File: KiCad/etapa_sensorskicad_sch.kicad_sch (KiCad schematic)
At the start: 15 parts, among them K1 Fujitsu_FTR-LYAA005x, K2 Fujitsu_FTR-LYAA005x, Q1 IRLIZ44N, U1 FDC2214, U2 FXTH87

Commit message: MANTECAMANTECOSA
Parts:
- renumbered U1 to U6, U2 to U7
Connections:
- net at U6.10 (IN0B): now also C3.1, L1.1
- net at U6.9 (IN0A): now also C3.2, L1.2
- net Vcc_12V renamed +12V
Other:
- moved on the sheet: C3, L1

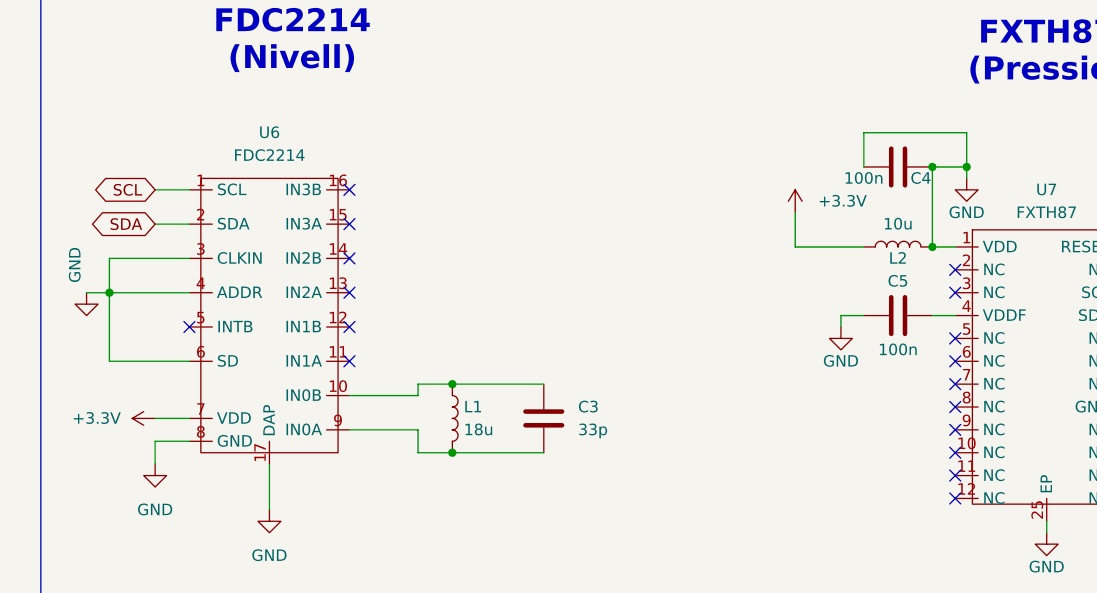
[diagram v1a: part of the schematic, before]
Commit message: GNDs, VCCs col.locats correctament, pull-ups, etc ben connectats
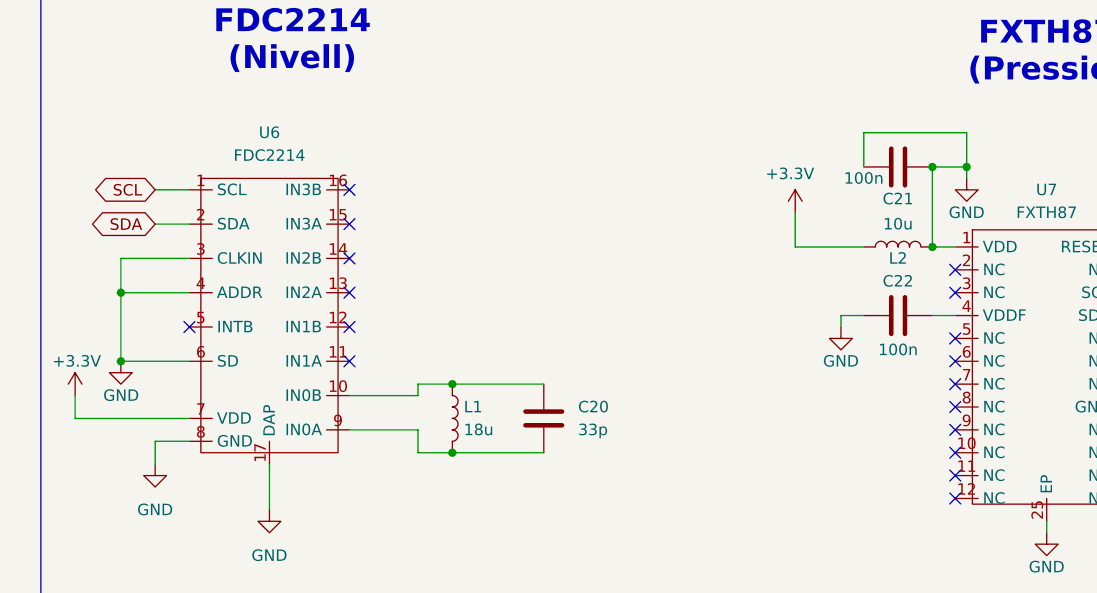
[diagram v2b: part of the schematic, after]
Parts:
- renumbered C3 to C20, C4 to C21, C5 to C22
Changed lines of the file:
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@@
+	)
+	(junction
+		(at 24.13 68.58)
+		(diameter 0)
+		(color 0 0 0 0)
 	)
 	(junction
@@
 	)
 	(junction
+		(at 24.13 60.96)
+		(diameter 0)
+		(color 0 0 0 0)
+	)
+	(junction
 		(at 118.11 46.99)
 		(diameter 0)
@@
 		(color 0 0 0 0)
 	)
-	(junction
-		(at 22.86 60.96)
-		(diameter 0)
-		(color 0 0 0 0)
-	)
 	(no_connect
 		(at 116.84 81.28)
@@
 	(wire
 		(pts
+			(xy 19.05 72.39) (xy 19.05 74.93)
+		)
+		(stroke
+			(width 0)
+			(type default)
+		)
+	)
+	(wire
+		(pts
 			(xy 226.06 139.7) (xy 251.46 139.7)
 		)
@@
 	(wire
 		(pts
-			(xy 31.75 68.58) (xy 22.86 68.58)
+			(xy 31.75 68.58) (xy 24.13 68.58)
 		)
 		(stroke
@@
 	(wire
 		(pts
-			(xy 31.75 57.15) (xy 22.86 57.15)
-		)
-		(stroke
-			(width 0)
-			(type default)
-		)
-	)
-	(wire
-		(pts
-			(xy 22.86 60.96) (xy 22.86 68.58)
+			(xy 31.75 57.15) (xy 24.13 57.15)
 		)
 		(stroke
@@
 	(wire
 		(pts
-			(xy 20.32 60.96) (xy 22.86 60.96)
+			(xy 24.13 60.96) (xy 24.13 68.58)
 		)
 		(stroke
@@
 	(wire
 		(pts
+			(xy 19.05 74.93) (xy 31.75 74.93)
+		)
+		(stroke
+			(width 0)
+			(type default)
+		)
+	)
+	(wire
+		(pts
 			(xy 99.06 52.07) (xy 99.06 55.88)
 		)
@@
 	(wire
 		(pts
-			(xy 22.86 57.15) (xy 22.86 60.96)
+			(xy 24.13 57.15) (xy 24.13 60.96)
 		)
 		(stroke
@@
 		)
 	)
+	(wire
+		(pts
+			(xy 24.13 60.96) (xy 31.75 60.96)
+		)
+		(stroke
+			(width 0)
+			(type default)
+		)
+	)
 	(bus
 		(pts
@@
 	(wire
 		(pts
-			(xy 27.94 74.93) (xy 31.75 74.93)
-		)
-		(stroke
-			(width 0)
-			(type default)
-		)
-	)
-	(wire
-		(pts
 			(xy 201.93 54.61) (xy 214.63 54.61)
 		)
@@
 		(pts
 			(xy 201.93 77.47) (xy 208.28 77.47)
-		)
-		(stroke
-			(width 0)
-			(type default)
-		)
-	)
-	(wire
-		(pts
-			(xy 22.86 60.96) (xy 31.75 60.96)
 		)
 		(stroke
@@
 		(on_board yes)
 		(dnp no)
-		(property "Reference" "C5"
+		(property "Reference" "C22"
 			(at 110.49 59.69 90)
 			(effects
@@
 			(project ""
 				(path "/27a7fca5-115a-450a-aa60-496c314f6c0e/214c85b5-e11a-40fa-b086-a325260ddb4b"
-					(reference "C5")
+					(reference "C22")
 					(unit 1)
 				)
@@
 		(on_board yes)
 		(dnp no)
-		(fields_autoplaced yes)
 		(property "Reference" "#PWR0121"
 			(at 99.06 55.88 0)
@@
 		)
 		(property "Value" "+3.3V"
-			(at 101.6 50.7999 0)
+			(at 95.758 47.752 0)
 			(effects
 				(font
@@
 	(symbol
 		(lib_id "power:GND")
-		(at 20.32 60.96 0)
+		(at 24.13 68.58 0)
 		(unit 1)
 		(exclude_from_sim no)
@@
 		(dnp no)
 		(property "Reference" "#PWR0109"
-			(at 20.32 67.31 0)
+			(at 24.13 74.93 0)
 			(effects
 				(font
@@
 		)
 		(property "Value" "GND"
-			(at 19.05 55.88 90)
+			(at 26.162 72.39 0)
 			(effects
 				(font
@@
 		)
 		(property "Footprint" ""
-			(at 20.32 60.96 0)
+			(at 24.13 68.58 0)
 			(effects
 				(font
@@
 		)
 		(property "Datasheet" ""
-			(at 20.32 60.96 0)
+			(at 24.13 68.58 0)
 			(effects
 				(font
@@
 		)
 		(property "Description" "Power symbol creates a global label with name \"GND\" , ground"
-			(at 20.32 60.96 0)
+			(at 24.13 68.58 0)
 			(effects
 				(font
@@
 		(dnp no)
 		(fields_autoplaced yes)
-		(property "Reference" "C3"
+		(property "Reference" "C20"
 			(at 74.93 73.6599 0)
 			(effects
@@
 			(project ""
 				(path "/27a7fca5-115a-450a-aa60-496c314f6c0e/214c85b5-e11a-40fa-b086-a325260ddb4b"
-					(reference "C3")
+					(reference "C20")
 					(unit 1)
 				)
@@
 		(on_board yes)
 		(dnp no)
-		(property "Reference" "C4"
-			(at 113.03 48.26 90)
+		(property "Reference" "C21"
+			(at 110.49 50.546 90)
 			(effects
 				(font
@@
 			(project "PROJECTE_CASTRO_RIBAS"
 				(path "/27a7fca5-115a-450a-aa60-496c314f6c0e/214c85b5-e11a-40fa-b086-a325260ddb4b"
-					(reference "C4")
+					(reference "C21")
 					(unit 1)
 				)
@@
 	(symbol
 		(lib_id "power:+3.3V")
-		(at 27.94 74.93 90)
+		(at 19.05 72.39 0)
 		(unit 1)
 		(exclude_from_sim no)
@@
 		(on_board yes)
 		(dnp no)
-		(fields_autoplaced yes)
 		(property "Reference" "#PWR0110"
-			(at 31.75 74.93 0)
+			(at 19.05 76.2 0)
 			(effects
 				(font
@@
 		)
 		(property "Value" "+3.3V"
-			(at 24.13 74.9299 90)
+			(at 16.51 68.58 0)
 			(effects
 				(font
@@
 		)
 		(property "Footprint" ""
-			(at 27.94 74.93 0)
+			(at 19.05 72.39 0)
 			(effects
 				(font
@@
 		)
 		(property "Datasheet" ""
-			(at 27.94 74.93 0)
+			(at 19.05 72.39 0)
 			(effects
 				(font
@@
 		)
 		(property "Description" "Power symbol creates a global label with name \"+3.3V\""
-			(at 27.94 74.93 0)
-			(effects
-				(font
+			(at 19.05 72.39 0)
+			(effects
+				(font

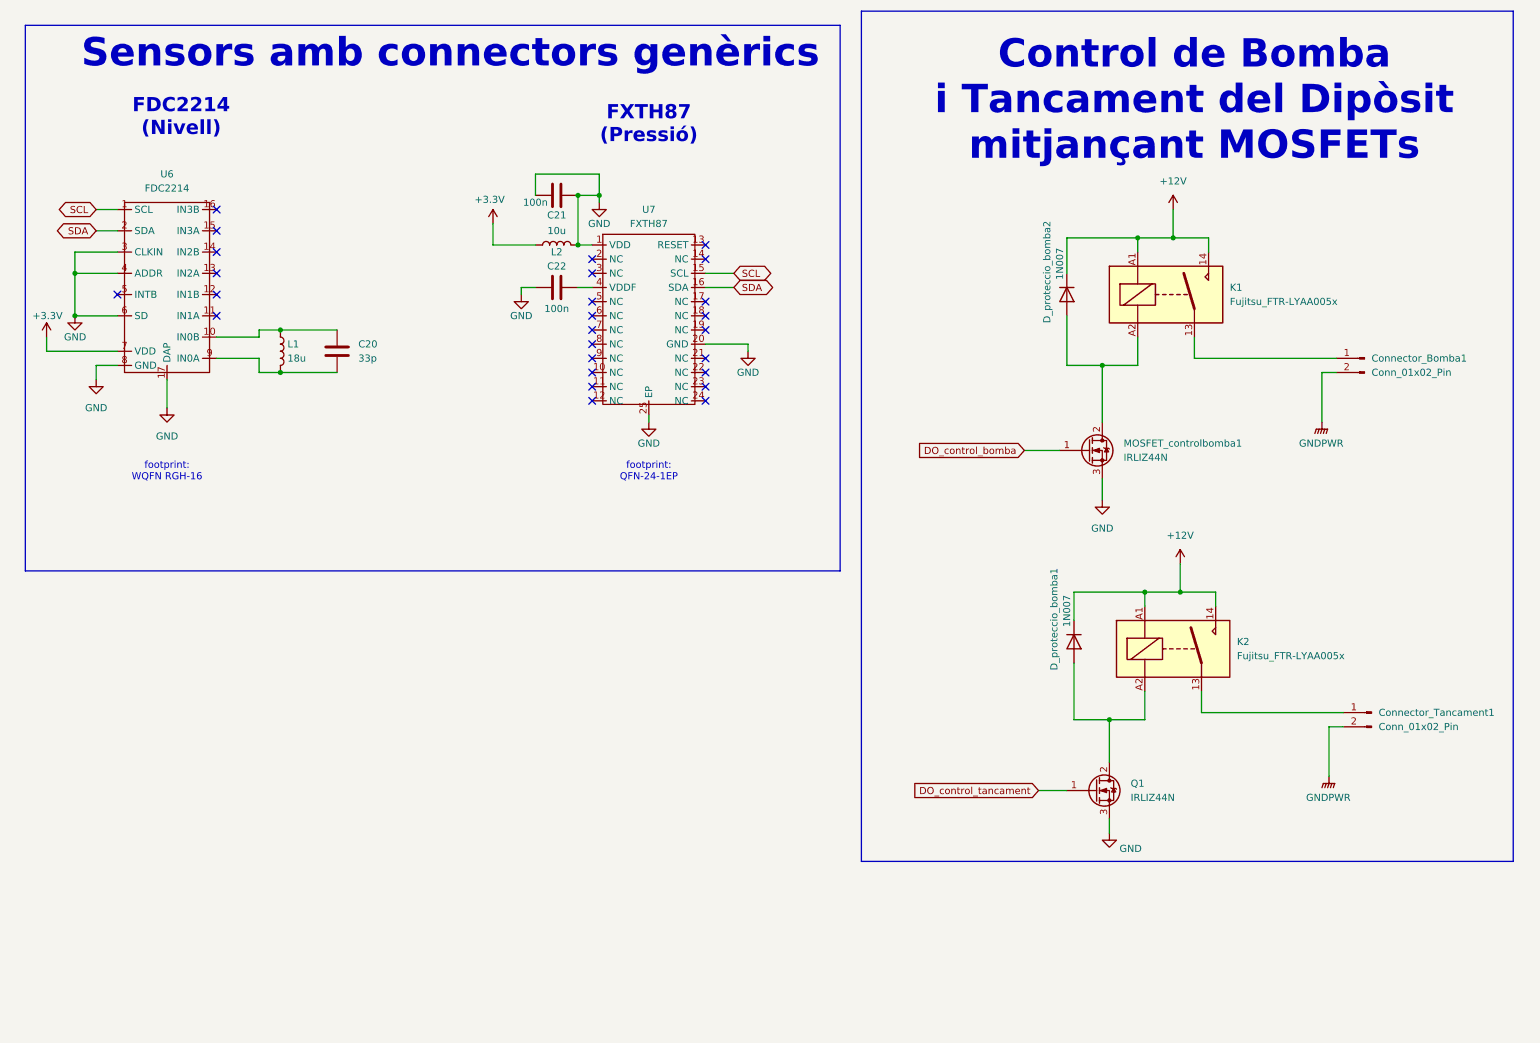
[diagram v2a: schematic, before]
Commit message: Afegides TOTES les petjades importants MENYS SENSOR de PRESSIO
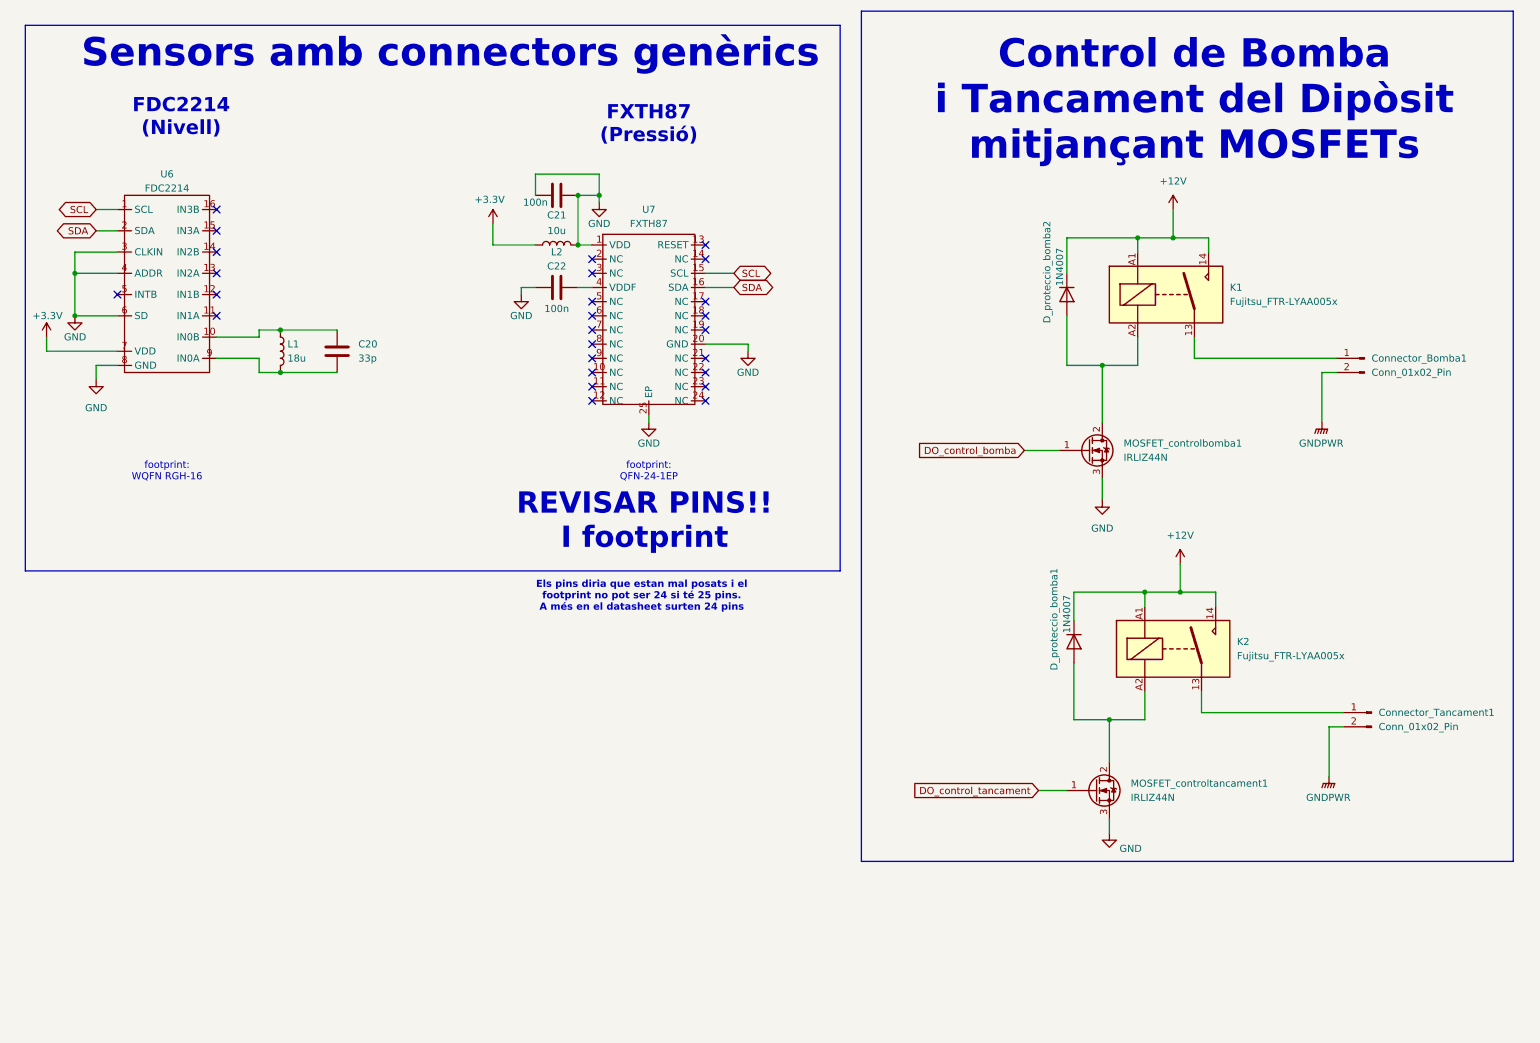
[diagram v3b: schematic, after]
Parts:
- D_proteccio_bomba1, D_proteccio_bomba2: value 1N007 -> 1N4007
- U6: footprint (none) -> Package_DFN_QFN:MPS_QFN-16_3x3mm_P0.5mm
- renumbered Q1 to MOSFET_controltancament1
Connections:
- net GND: no longer U6.17 (DAP)
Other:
- note added: "Els pins diria que estan mal posats i el footprint no pot ser 24 si té 25 pins. A més en el datasheet surten 24 pins"
- note added: "REVISAR PINS!! I footprint"
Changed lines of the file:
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@@
+		)
+	)
+	(text "Els pins diria que estan mal posats i el \nfootprint no pot ser 24 si té 25 pins.\nA més en el datasheet surten 24 pins"
+		(exclude_from_sim no)
+		(at 125.73 118.872 0)
+		(effects
+			(font
+				(size 1.27 1.27)
+				(thickness 0.254)
+				(bold yes)
+			)
 		)
 	)
@@
 		)
 	)
+	(text "REVISAR PINS!!\nI footprint"
+		(exclude_from_sim no)
+		(at 126.238 105.41 0)
+		(effects
+			(font
+				(size 3.81 3.81)
+				(thickness 1.016)
+				(bold yes)
+			)
+		)
+	)
 	(text "Control de Bomba\ni Tancament del Dipòsit\nmitjançant MOSFETs"
 		(exclude_from_sim no)
@@
 		(pts
 			(xy 228.6 120.65) (xy 228.6 118.11)
-		)
-		(stroke
-			(width 0)
-			(type default)
-		)
-	)
-	(wire
-		(pts
-			(xy 40.64 80.01) (xy 40.64 85.09)
 		)
 		(stroke
@@
 		)
 	)
+	(rule_area
+		(polyline
+			(pts
+				(xy 93.98 29.21) (xy 156.21 29.21) (xy 157.48 30.48) (xy 157.48 109.22) (xy 93.98 109.22)
+			)
+			(stroke
+				(width 0)
+				(type dash)
+			)
+			(fill
+				(type none)
+			)
+		)
+	)
 	(symbol
 		(lib_id "Relay:Fujitsu_FTR-LYAA005x")
@@
 			)
 		)
-		(property "Footprint" ""
+		(property "Footprint" "Package_DFN_QFN:MPS_QFN-16_3x3mm_P0.5mm"
 			(at 41.91 50.8 0)
 			(effects
@@
 		)
 		(pin "7"
-		)
-		(pin "17"
 		)
 		(pin "12"
@@
 	)
 	(symbol
-		(lib_id "power:GND")
-		(at 40.64 85.09 0)
-		(unit 1)
-		(exclude_from_sim no)
-		(in_bom yes)
-		(on_board yes)
-		(dnp no)
-		(property "Reference" "#PWR0112"
-			(at 40.64 91.44 0)
-			(effects
-				(font
-					(size 1.27 1.27)
-				)
-				(hide yes)
-			)
-		)
-		(property "Value" "GND"
-			(at 40.64 90.17 0)
-			(effects
-				(font
-					(size 1.27 1.27)
-				)
-			)
-		)
-		(property "Footprint" ""
-			(at 40.64 85.09 0)
-			(effects
-				(font
-					(size 1.27 1.27)
-				)
-				(hide yes)
-			)
-		)
-		(property "Datasheet" ""
-			(at 40.64 85.09 0)
-			(effects
-				(font
-					(size 1.27 1.27)
-				)
-				(hide yes)
-			)
-		)
-		(property "Description" "Power symbol creates a global label with name \"GND\" , ground"
-			(at 40.64 85.09 0)
-			(effects
-				(font
-					(size 1.27 1.27)
-				)
-				(hide yes)
-			)
-		)
-		(pin "1"
-		)
-		(instances
-			(project "PROJECTE_CASTRO_RIBAS"
-				(path "/27a7fca5-115a-450a-aa60-496c314f6c0e/214c85b5-e11a-40fa-b086-a325260ddb4b"
-					(reference "#PWR0112")
-					(unit 1)
-				)
-			)
-		)
-	)
-	(symbol
 		(lib_id "Transistor_FET:IRLIZ44N")
 		(at 205.74 92.71 0)
@@
 			)
 		)
-		(property "Value" "1N007"
+		(property "Value" "1N4007"
 			(at 200.66 56.388 0)
 			(effects
@@
 		(on_board yes)
 		(dnp no)
-		(property "Reference" "Q1"
+		(property "Reference" "MOSFET_controltancament1"
 			(at 213.36 152.3999 0)
 			(effects
@@
 			(project ""
 				(path "/27a7fca5-115a-450a-aa60-496c314f6c0e/214c85b5-e11a-40fa-b086-a325260ddb4b"
-					(reference "Q1")
+					(reference "MOSFET_controltancament1")
 					(unit 1)
 				)
@@
 			)
 		)
-		(property "Value" "1N007"
+		(property "Value" "1N4007"
 			(at 201.93 118.618 0)
 			(effects

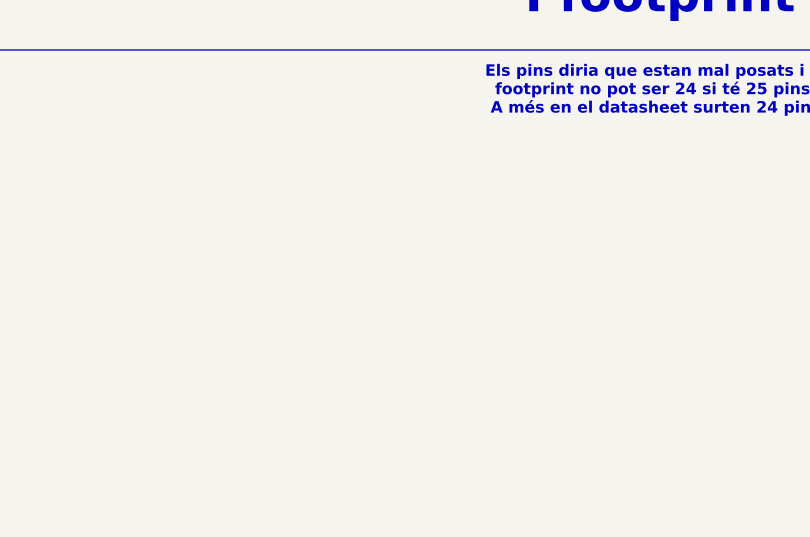
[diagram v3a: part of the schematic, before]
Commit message: Nou Símbol pel sensor de pressió FXTH87
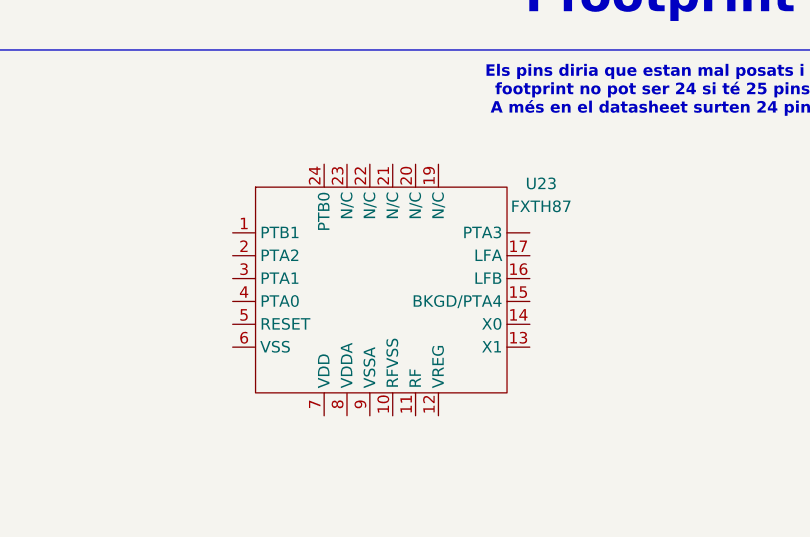
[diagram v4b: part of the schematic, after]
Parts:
- added U23: FXTH87, symbol FXTH87:FXTH87
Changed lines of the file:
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@@
+	)
+	(symbol
+		(lib_id "FXTH87:FXTH87")
+		(at 95.25 140.97 0)
+		(unit 1)
+		(exclude_from_sim no)
+		(in_bom yes)
+		(on_board yes)
+		(dnp no)
+		(fields_autoplaced yes)
+		(property "Reference" "U23"
+			(at 113.03 129.1746 0)
+			(effects
+				(font
+					(size 1.27 1.27)
+				)
+			)
+		)
+		(property "Value" "FXTH87"
+			(at 113.03 131.7146 0)
+			(effects
+				(font
+					(size 1.27 1.27)
+				)
+			)
+		)
+		(property "Footprint" ""
+			(at 95.25 140.97 0)
+			(effects
+				(font
+					(size 1.27 1.27)
+				)
+				(hide yes)
+			)
+		)
+		(property "Datasheet" ""
+			(at 95.25 140.97 0)
+			(effects
+				(font
+					(size 1.27 1.27)
+				)
+				(hide yes)
+			)
+		)
+		(property "Description" ""
+			(at 95.25 140.97 0)
+			(effects
+				(font
+					(size 1.27 1.27)
+				)
+				(hide yes)
+			)
+		)
+		(pin "11"
+		)
+		(pin "12"
+		)
+		(pin "21"
+		)
+		(pin "9"
+		)
+		(pin "8"
+		)
+		(pin "13"
+		)
+		(pin "1"
+		)
+		(pin "7"
+		)
+		(pin "10"
+		)
+		(pin "3"
+		)
+		(pin ""
+		)
+		(pin "24"
+		)
+		(pin "22"
+		)
+		(pin "6"
+		)
+		(pin "2"
+		)
+		(pin "4"
+		)
+		(pin "5"
+		)
+		(pin "23"
+		)
+		(pin "20"
+		)
+		(pin "19"
+		)
+		(pin "17"
+		)
+		(pin "16"
+		)
+		(pin "15"
+		)
+		(pin "14"
+		)
+		(instances
+			(project ""
+				(path "/27a7fca5-115a-450a-aa60-496c314f6c0e/214c85b5-e11a-40fa-b086-a325260ddb4b"
+					(reference "U23")
+					(unit 1)
+				)
+			)
+		)
 	)
 	(symbol

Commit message: Més FXTH87, alguna petjada més, i molts dubtes
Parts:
- added C32, C33: 100nF, symbol Device:C
- added FB2: FerriteBead, Inductor_SMD:L_1812_4532Metric, symbol Device:FerriteBead
- added J5: Conn_01x04_Pin, Connector_PinHeader_2.54mm:PinHeader_1x04_P2.54mm_Vertical, symbol Connector:Conn_01x04_Pin
- Connector_Bomba1, Connector_Tancament1: footprint (none) -> Connector_PinHeader_2.54mm:PinHeader_1x02_P2.54mm_Vertical
- U23: footprint (none) -> Package_DFN_QFN:UDC-QFN-20-4EP_3x4mm_P0.5mm_EP0.41x0.25mm
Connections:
- net +3.3V: now also U23.7 (VDD), FB2.2, J5.2 (Pin_2)
- net GND: now also U23.10 (RFVSS), U23.6 (VSS), U23.9 (VSSA), C33.2, J5.3 (Pin_3)
- net at U23.12 (VREG): now also C33.1
- net Programador: now reaches U23.15 (BKGD/PTA4)
- net Programador: now also J5.1 (Pin_1)
- net RB9: now reaches U23.3 (PTA1)
- net RB8: now reaches U23.4 (PTA0)
- net Reset: now reaches U23.5 (RESET)
- net Reset: now also J5.4 (Pin_4)
- net at U23.8 (VDDA): now also C32.1
- new net: C32.2, FB2.1
- no-connect marks 26 -> 39
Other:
- note added: "Programador de Sensor de Pressió"
